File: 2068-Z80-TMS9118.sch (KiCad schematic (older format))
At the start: 39 parts, among them J1 RCJ-014, J2 Conn_02x20_Counter_Clockwise, J3 DB9_Male_MountingHoles, J4 DB9_Male_MountingHoles, J5 Conn_02x10_Odd_Even, J6 Conn_01x02, Q3 2N4401, U1 TMS4416, U2 TMS4416, U3 TMS9118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

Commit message: Change schematic to as-built bodged Rev 0
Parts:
- removed R1: 10, Resistor_THT:R_Axial_DIN0204_L3.6mm_D1.6mm_P5.08mm_Horizontal, symbol Device:R
- removed R2: 10K, Resistor_THT:R_Axial_DIN0204_L3.6mm_D1.6mm_P5.08mm_Horizontal, symbol Device:R
- removed R4: 330, Resistor_THT:R_Axial_DIN0204_L3.6mm_D1.6mm_P5.08mm_Horizontal, symbol Device:R
- added C11: 470pF, Capacitor_THT:C_Disc_D3.8mm_W2.6mm_P2.50mm, symbol Device:C_Small
- added C12, C13: .1uF, Capacitor_THT:C_Disc_D3.8mm_W2.6mm_P2.50mm, symbol Device:C_Small
- added FB1: Ferrite_Bead_Small, Resistor_THT:R_Axial_DIN0204_L3.6mm_D1.6mm_P5.08mm_Horizontal, symbol Device:Ferrite_Bead_Small
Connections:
- net +5V: now also C12.1, C13.1, FB1.1; no longer J3.5, J4.5
- net A8_1: no longer J3.7
- net A9_1: no longer J4.7
- net GND: now also C11.2, C12.2, C13.2; no longer J3.9, J4.9
- net NTSC: now also C11.1
- net at C8.1, C9.1, Q3.3 (C): now also FB1.2
- no-connect marks 30 -> 36
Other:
- note added: "Copyright (C) 2022 John Winans\n\nThis documentation describes Open Hardware and is licensed under the CERN OHL v. 1.2.\n\nYou may redistribute and modify this documentation under the terms of the CERN OHL v.1.2. (http://ohwr.org/cernohl). \nThis documentation is distributed WITHOUT ANY EXPRESS OR IMPLIED WARRANTY, INCLUDING OF MERCHANTABILITY, \nSATISFACTORY QUALITY AND FITNESS FOR A PARTICULAR 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"
- note added: "Down"
- note added: "Fire"
- note added: "Left"
- note added: "Right"
- note added: "Up"
- note removed: "Copyright (C) 2021 John Winans\n\nThis documentation describes Open Hardware and is licensed under the CERN OHL v. 1.2.\n\nYou may redistribute and modify this documentation under the terms of the CERN OHL v.1.2. (http://ohwr.org/cernohl). \nThis documentation is distributed WITHOUT ANY EXPRESS OR IMPLIED WARRANTY, INCLUDING OF MERCHANTABILITY, \nSATISFACTORY QUALITY AND FITNESS FOR A PARTICULAR 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"
- note removed: "Do not populate R2"
- moved on the sheet: J3, J4, J5

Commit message: Added first draft BOM for Rev 1
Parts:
- C1, C10, C12, C13, C2, C3, C6, C8: MPN (none) -> C315C104M5U5TA7303; Manufacturer (none) -> KEMET
- C11: Description CAP CER 0.1UF 50V Z5U RADIAL -> CAP CER 470PF 10% 100V C0G RAD; Digi-Key_PN 399-9859-1-ND‎ -> 399-13987-ND; MPN (none) -> C315C471K1G5TA; Manufacturer (none) -> KEMET
- C4, C5: Description CAP CER 0.1UF 50V Z5U RADIAL -> CAP CER 27PF 10% 200V C0G RADIAL; Digi-Key_PN 399-9859-1-ND‎ -> 399-13983-ND; MPN (none) -> C315C270K2G5TA; Manufacturer (none) -> KEMET
- C7: Description (none) -> 470 µF 10 V Aluminum Electrolytic Capacitors Radial, Can 54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; Digi-Key_PN (none) -> 338-1709-ND; MPN (none) -> SK471M010ST; Manufacturer (none) -> Cornell Dubilier Electronics (CDE)
- C9: Manufacturer (none) -> Panasonic Electronic Components
- D1: Description (none) -> DIODE GEN PURP 100V 200MA DO35; Digi-Key_PN (none) -> 1N914CT-ND; MPN (none) -> 1N914TR; Manufacturer (none) -> onsemi
- FB1: Description (none) -> FERRITE BEAD 50 OHM AXIAL 1LN; Digi-Key_PN (none) -> P9820BK-ND; MPN (none) -> EXC-ELSA35; Manufacturer (none) -> Panasonic Electronic Components
- J2: Description Female connector, double row, 02x20 -> 2 x 20 (40 Pin) Extra Tall Female 0.1 Inch Pitch Stacking H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; Digi-Key_PN S6104-ND -> (none); MPN PPTC202LFBN-RC -> (none); Manufacturer Sullins Connector Solutions -> (none)
- J3, J4: Description (none) -> 9 Position D-Sub Plug, Male Pins Connector; Digi-Key_PN (none) -> AE10970-ND; MPN (none) -> A-DS 09 A/KG-T4S; Manufacturer (none) -> Assmann WSW Components
- J5: Description (none) -> CONN HEADER VERT 20POS 2.54MM; Digi-Key_PN (none) -> 2057-PH2-20-UA-ND; MPN (none) -> PH2-20-UA; Manufacturer (none) -> Adam Tech
- J6: Description (none) -> CONN HEADER VERT 2POS 2.54MM; Digi-Key_PN (none) -> 2057-PH1-02-UA-ND; MPN (none) -> PH1-02-UA; Manufacturer (none) -> Adam Tech
- Q3: Description NPN transistor -> TRANS NPN 40V 0.6A TO92-3; Digi-Key_PN (none) -> 2N4401TFCT-ND; MPN (none) -> 2N4401TF; Manufacturer (none) -> onsemi
- R3: Description RES 1K OHM 5% 1/8W AXIAL -> RES 33 OHM 5% 1/8W AXIAL; Digi-Key_PN CF18JT1K00CT-ND -> CF18JT33R0CT-ND; MPN CF18JT1K00 -> CF18JT33R0
- R7: Description RES 1K OHM 5% 1/8W AXIAL -> RES 470 OHM 5% 1/8W AXIAL; Digi-Key_PN CF18JT1K00CT-ND -> CF18JT470RCT-ND; MPN CF18JT1K00 -> CF18JT470R
- RN1, RN2: Description (none) -> RES ARRAY 8 RES 10K OHM 9SIP; Digi-Key_PN (none) -> 4609X-101-103LF-ND; MPN (none) -> 4609X-101-103LF; Manufacturer (none) -> Bourns Inc.
- U1, U2, U3: MPN (none) -> EBAY
- U4, U5: Description (none) -> IC DECODER/DEMUX 1X3:8 16DIP; Digi-Key_PN (none) -> 296-1639-5-ND; MPN (none) -> SN74LS138N; Manufacturer (none) -> Texas Instruments
- U6, U7: Description (none) -> IC BUF NON-INVERT 5.25V 20DIP; Digi-Key_PN (none) -> 296-1653-5-ND; MPN (none) -> SN74LS244N; Manufacturer (none) -> Texas Instruments
- Y1: Description (none) -> CRYSTAL 10.738635MHZ 32PF TH; Manufacturer (none) -> CTS-Frequency Controls

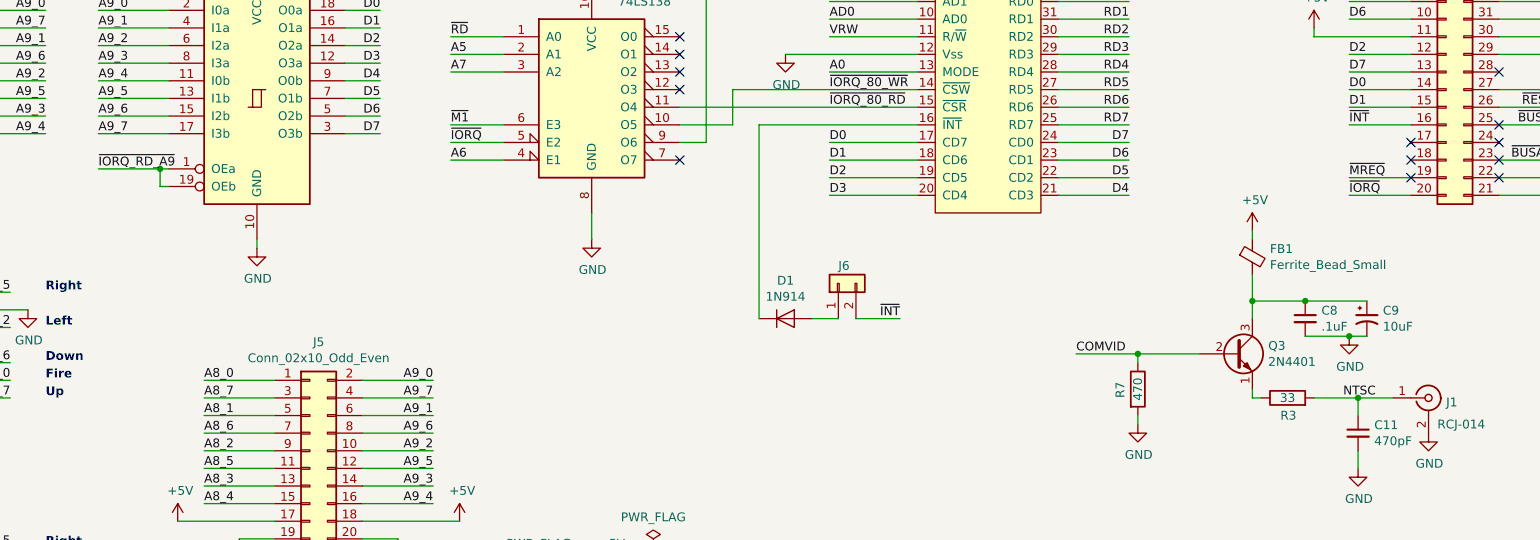
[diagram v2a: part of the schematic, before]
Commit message: Added J7 and replace J6 (to include NMI)
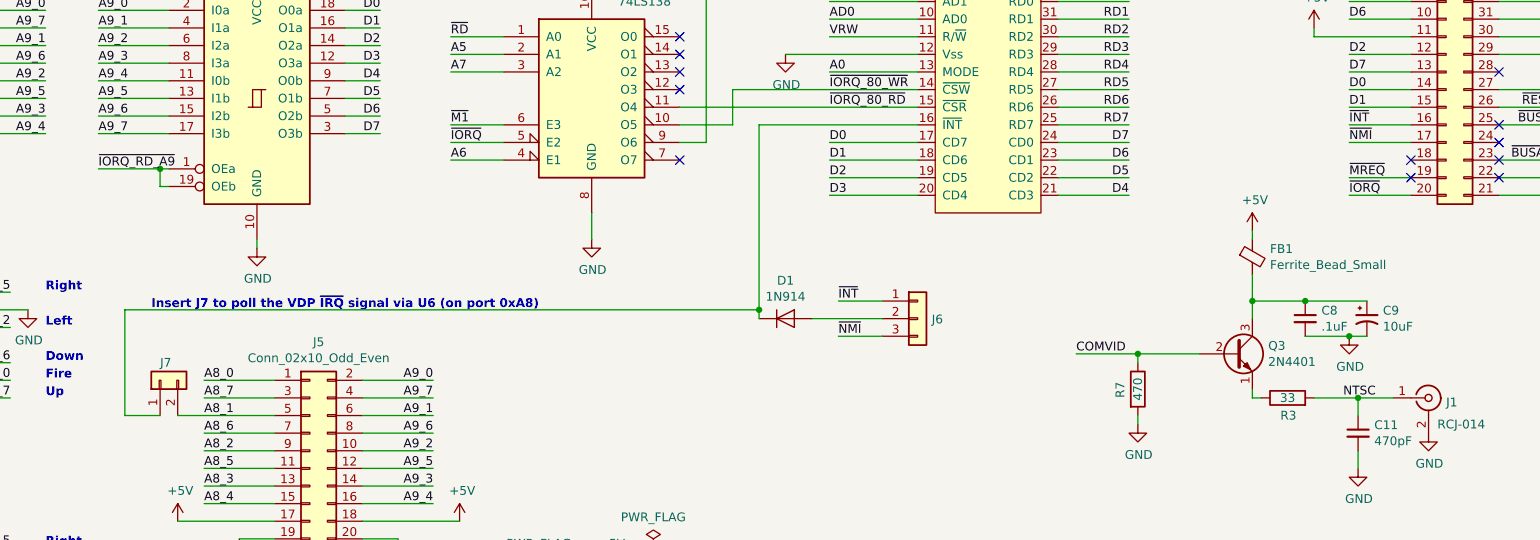
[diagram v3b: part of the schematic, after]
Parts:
- removed J6: Conn_01x02, Connector_PinHeader_2.54mm:PinHeader_1x02_P2.54mm_Vertical, symbol Connector_Generic:Conn_01x02
- added J6: Conn_01x03, Connector_PinHeader_2.54mm:PinHeader_1x03_P2.54mm_Vertical, symbol Connector_Generic:Conn_01x03
- added J7: Conn_01x02, Connector_PinHeader_2.54mm:PinHeader_1x02_P2.54mm_Vertical, symbol Connector_Generic:Conn_01x02
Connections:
- net A8_1: now also J7.2 (Pin_2)
- net ~INT: now also J6.1 (Pin_1)
- net ~NMI: now reaches J2.17 (Pin_17)
- net ~NMI: now also J6.3 (Pin_3)
- net at D1.1 (K), U3.16 (~INT): now also J7.1 (Pin_1)
- net at D1.2 (A): now also J6.2 (Pin_2)
- no-connect marks 36 -> 35
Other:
- note added: "Insert J7 to poll the VDP ~IRQ~ signal via U6 (on port 0xA8)"
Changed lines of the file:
@@
 Sheet 1 1
 Title "TMS9118 Video & Joysticks"
-Date "2021-09-05"
-Rev "1"
+Date "2023-05-20"
+Rev "2"
 Comp ""
 Comment1 ""
@@
 NoConn ~ 9750 4400
 NoConn ~ 9250 4500
-NoConn ~ 9250 4400
 NoConn ~ 9250 3300
 $Comp
@@
 Wire Wire Line
 	2800 6450 2400 6450
-Wire Wire Line
-	2400 5950 2800 5950
 Text Label 2400 5750 0    50   ~ 0
 A8_0
@@
 Text Label 8900 4300 0    50   ~ 0
 ~INT
-Text Label 6350 5400 2    50   ~ 0
+Text Label 6000 5300 0    50   ~ 0
 ~INT
 $Comp
@@
 $EndComp
 Wire Wire Line
-	5850 5400 6000 5400
-Wire Wire Line
-	5550 5400 5550 4300
+	5550 5400 5550 5350
 Wire Wire Line
 	5550 4300 6450 4300
-$Comp
-L Connector_Generic:Conn_01x02 J6
-U 1 1 64FA6625
-P 6000 5200
-F 0 "J6" V 6100 5200 50  0000 R CNN
-F 1 "Conn_01x02" V 5873 5012 50  0001 R CNN
-F 2 "Connector_PinHeader_2.54mm:PinHeader_1x02_P2.54mm_Vertical" H 6000 5200 50  0001 C CNN
-F 3 "https://app.adam-tech.com/products/download/data_sheet/201605/ph1-xx-ua-data-sheet.pdf" H 6000 5200 50  0001 C CNN
-F 4 "CONN HEADER VERT 2POS 2.54MM" H 6000 5200 50  0001 C CNN "Description"
-F 5 "2057-PH1-02-UA-ND" H 6000 5200 50  0001 C CNN "Digi-Key_PN"
-F 6 "PH1-02-UA" H 6000 5200 50  0001 C CNN "MPN"
-F 7 "Adam Tech" H 6000 5200 50  0001 C CNN "Manufacturer"
-	1    6000 5200
-	0    -1   -1   0
-$EndComp
-Wire Wire Line
-	6100 5400 6350 5400
+Wire Wire Line
+	6250 5300 6000 5300
 Wire Wire Line
 	2200 1400 1800 1400
@@
 	2650 7600 2300 7600
 Connection ~ 2650 7600
+$Comp
+L Connector_Generic:Conn_01x02 J7
+U 1 1 646B8B12
+P 2150 5750
+F 0 "J7" V 2250 5750 50  0000 R CNN
+F 1 "Conn_01x02" V 2023 5562 50  0001 R CNN
+F 2 "Connector_PinHeader_2.54mm:PinHeader_1x02_P2.54mm_Vertical" H 2150 5750 50  0001 C CNN
+F 3 "https://app.adam-tech.com/products/download/data_sheet/201605/ph1-xx-ua-data-sheet.pdf" H 2150 5750 50  0001 C CNN
+F 4 "CONN HEADER VERT 2POS 2.54MM" H 2150 5750 50  0001 C CNN "Description"
+F 5 "2057-PH1-02-UA-ND" H 2150 5750 50  0001 C CNN "Digi-Key_PN"
+F 6 "PH1-02-UA" H 2150 5750 50  0001 C CNN "MPN"
+F 7 "Adam Tech" H 2150 5750 50  0001 C CNN "Manufacturer"
+	1    2150 5750
+	0    -1   -1   0
+$EndComp
+Wire Wire Line
+	2250 5950 2800 5950
+Wire Wire Line
+	2150 5950 1950 5950
+Wire Wire Line
+	1950 5950 1950 5350
+Wire Wire Line
+	1950 5350 5550 5350
+Connection ~ 5550 5350
+Wire Wire Line
+	5550 5350 5550 4300
+Text Notes 2100 5350 0    50   ~ 10
+Insert J7 to poll the VDP ~IRQ~ signal via U6 (on port 0xA8)
+$Comp
+L Connector_Generic:Conn_01x03 J6
+U 1 1 647F010F
+P 6450 5400
+F 0 "J6" H 6530 5396 50  0000 L CNN
+F 1 "Conn_01x03" V 6323 5212 50  0001 R CNN
+F 2 "Connector_PinHeader_2.54mm:PinHeader_1x03_P2.54mm_Vertical" H 6450 5400 50  0001 C CNN
+F 3 "~" H 6450 5400 50  0001 C CNN
+	1    6450 5400
+	1    0    0    -1
+$EndComp
+Wire Wire Line
+	5850 5400 6250 5400
+Text Label 6000 5500 0    50   ~ 0
+~NMI
+Wire Wire Line
+	6250 5500 6000 5500
+Wire Wire Line
+	9250 4400 8900 4400
+Text Label 8900 4400 0    50   ~ 0
+~NMI
 $EndSCHEMATC

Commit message: Add support for MSX joysticks
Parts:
- added J8, J9: Conn_01x02, Connector_PinHeader_2.54mm:PinHeader_1x02_P2.54mm_Vertical, symbol Connector_Generic:Conn_01x02
- added R1: 100, Resistor_THT:R_Axial_DIN0207_L6.3mm_D2.5mm_P10.16mm_Horizontal, symbol Device:R
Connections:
- net +5V: now also R1.2
- net A8_4: now also J3.7
- net A9_4: now also J4.7
- net GND: now also J3.9, J4.9
- net at J3.5: now also J9.1 (Pin_1)
- net at J4.5: now also J8.1 (Pin_1)
- new net: J8.2 (Pin_2), J9.2 (Pin_2), R1.1
- no-connect marks 35 -> 29
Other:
- note added: "Btn 2"
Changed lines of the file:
@@
 Sheet 1 1
 Title "TMS9118 Video & Joysticks"
-Date "2023-05-20"
-Rev "2"
+Date "2023-06-03"
+Rev "2.1"
 Comp ""
 Comment1 ""
@@
 Text Label 1500 2100 2    50   ~ 0
 A8_4
-$Comp
-L Connector:DB9_Male_MountingHoles J4
-U 1 1 63B67655
-P 750 6900
-F 0 "J4" H 800 7400 50  0000 C CNN
-F 1 "DB9_Male_MountingHoles" H 930 6900 50  0001 L CNN
-F 2 "Connector_Dsub:DSUB-9_Male_Horizontal_P2.77x2.84mm_EdgePinOffset7.70mm_Housed_MountingHolesOffset9.12mm" H 750 6900 50  0001 C CNN
-F 3 "http://www.assmann-wsw.com/uploads/datasheets/ASS_4888_CO.pdf" H 750 6900 50  0001 C CNN
-F 4 "9 Position D-Sub Plug, Male Pins Connector" H 750 6900 50  0001 C CNN "Description"
-F 5 "AE10970-ND" H 750 6900 50  0001 C CNN "Digi-Key_PN"
-F 6 "A-DS 09 A/KG-T4S" H 750 6900 50  0001 C CNN "MPN"
-F 7 "Assmann WSW Components" H 750 6900 50  0001 C CNN "Manufacturer"
-	1    750  6900
-	-1   0    0    -1
-$EndComp
 Wire Wire Line
 	1500 3750 1100 3750
@@
 $EndComp
 Wire Wire Line
-	1050 5350 1400 5350
-Wire Wire Line
-	1050 6800 1400 6800
+	1050 5350 1100 5350
+Wire Wire Line
+	1050 6800 1100 6800
 Wire Wire Line
 	1050 6700 1300 6700
@@
 Text Notes 1500 5850 0    50   ~ 10
 Up
-NoConn ~ 1050 5550
-NoConn ~ 1050 5150
-$Comp
-L Connector:DB9_Male_MountingHoles J3
-U 1 1 6392BF40
-P 750 5450
-F 0 "J3" H 800 5950 50  0000 C CNN
-F 1 "DB9_Male_MountingHoles" H 930 5450 50  0001 L CNN
-F 2 "Connector_Dsub:DSUB-9_Male_Horizontal_P2.77x2.84mm_EdgePinOffset7.70mm_Housed_MountingHolesOffset9.12mm" H 750 5450 50  0001 C CNN
-F 3 "http://www.assmann-wsw.com/uploads/datasheets/ASS_4888_CO.pdf" H 750 5450 50  0001 C CNN
-F 4 "9 Position D-Sub Plug, Male Pins Connector" H 750 5450 50  0001 C CNN "Description"
-F 5 "AE10970-ND" H 750 5450 50  0001 C CNN "Digi-Key_PN"
-F 6 "A-DS 09 A/KG-T4S" H 750 5450 50  0001 C CNN "MPN"
-F 7 "Assmann WSW Components" H 750 5450 50  0001 C CNN "Manufacturer"
-	1    750  5450
-	-1   0    0    -1
-$EndComp
-NoConn ~ 1050 5050
 Text Notes 1500 5650 0    50   ~ 10
 Down
@@
 Text Notes 1500 7200 0    50   ~ 10
 Fire
-NoConn ~ 1050 6500
-NoConn ~ 1050 6600
-NoConn ~ 1050 7000
 Wire Wire Line
 	7700 5600 8050 5600
@@
 Text Label 8900 4400 0    50   ~ 0
 ~NMI
+$Comp
+L Connector_Generic:Conn_01x02 J8
+U 1 1 64804C73
+P 1200 6250
+F 0 "J8" V 1300 6250 50  0000 R CNN
+F 1 "Conn_01x02" V 1073 6062 50  0001 R CNN
+F 2 "Connector_PinHeader_2.54mm:PinHeader_1x02_P2.54mm_Vertical" H 1200 6250 50  0001 C CNN
+F 3 "https://app.adam-tech.com/products/download/data_sheet/201605/ph1-xx-ua-data-sheet.pdf" H 1200 6250 50  0001 C CNN
+F 4 "CONN HEADER VERT 2POS 2.54MM" H 1200 6250 50  0001 C CNN "Description"
+F 5 "2057-PH1-02-UA-ND" H 1200 6250 50  0001 C CNN "Digi-Key_PN"
+F 6 "PH1-02-UA" H 1200 6250 50  0001 C CNN "MPN"
+F 7 "Adam Tech" H 1200 6250 50  0001 C CNN "Manufacturer"
+	1    1200 6250
+	0    -1   -1   0
+$EndComp
+$Comp
+L Connector:DB9_Male_MountingHoles J4
+U 1 1 63B67655
+P 750 6900
+F 0 "J4" H 800 7400 50  0000 C CNN
+F 1 "DB9_Male_MountingHoles" H 930 6900 50  0001 L CNN
+F 2 "Connector_Dsub:DSUB-9_Male_Horizontal_P2.77x2.84mm_EdgePinOffset7.70mm_Housed_MountingHolesOffset9.12mm" H 750 6900 50  0001 C CNN
+F 3 "http://www.assmann-wsw.com/uploads/datasheets/ASS_4888_CO.pdf" H 750 6900 50  0001 C CNN
+F 4 "9 Position D-Sub Plug, Male Pins Connector" H 750 6900 50  0001 C CNN "Description"
+F 5 "AE10970-ND" H 750 6900 50  0001 C CNN "Digi-Key_PN"
+F 6 "A-DS 09 A/KG-T4S" H 750 6900 50  0001 C CNN "MPN"
+F 7 "Assmann WSW Components" H 750 6900 50  0001 C CNN "Manufacturer"
+	1    750  6900
+	-1   0    0    -1
+$EndComp
+$Comp
+L Connector:DB9_Male_MountingHoles J3
+U 1 1 6392BF40
+P 750 5450
+F 0 "J3" H 800 5950 50  0000 C CNN
+F 1 "DB9_Male_MountingHoles" H 930 5450 50  0001 L CNN
+F 2 "Connector_Dsub:DSUB-9_Male_Horizontal_P2.77x2.84mm_EdgePinOffset7.70mm_Housed_MountingHolesOffset9.12mm" H 750 5450 50  0001 C CNN
+F 3 "http://www.assmann-wsw.com/uploads/datasheets/ASS_4888_CO.pdf" H 750 5450 50  0001 C CNN
+F 4 "9 Position D-Sub Plug, Male Pins Connector" H 750 5450 50  0001 C CNN "Description"
+F 5 "AE10970-ND" H 750 5450 50  0001 C CNN "Digi-Key_PN"
+F 6 "A-DS 09 A/KG-T4S" H 750 5450 50  0001 C CNN "MPN"
+F 7 "Assmann WSW Components" H 750 5450 50  0001 C CNN "Manufacturer"
+	1    750  5450
+	-1   0    0    -1
+$EndComp
+Wire Wire Line
+	1050 6500 1200 6500
+Wire Wire Line
+	1200 6500 1200 6450
+Wire Wire Line
+	1300 6450 1400 6450
+$Comp
+L power:+5V #PWR0124
+U 1 1 6485FD29
+P 1950 6450
+F 0 "#PWR0124" H 1950 6300 50  0001 C CNN
+F 1 "+5V" H 1965 6623 50  0000 C CNN
+F 2 "" H 1950 6450 50  0001 C CNN
+F 3 "" H 1950 6450 50  0001 C CNN
+	1    1950 6450
+	1    0    0    -1
+$EndComp
+$Comp
+L Device:R R1
+U 1 1 648995F2
+P 1700 6450
+F 0 "R1" V 1600 6400 50  0000 L CNN
+F 1 "100" V 1700 6450 50  0000 C CNN
+F 2 "Resistor_THT:R_Axial_DIN0207_L6.3mm_D2.5mm_P10.16mm_Horizontal" V 1630 6450 50  0001 C CNN
+F 3 "https://www.seielect.com/catalog/sei-cf_cfm.pdf" H 1700 6450 50  0001 C CNN
+F 4 "RES 33 OHM 5% 1/8W AXIAL" H 1700 6450 50  0001 C CNN "Description"
+F 5 "CF18JT33R0CT-ND" H 1700 6450 50  0001 C CNN "Digi-Key_PN"
+F 6 "CF18JT33R0" H 1700 6450 50  0001 C CNN "MPN"
+F 7 "Stackpole Electronics Inc" H 1700 6450 50  0001 C CNN "Manufacturer"
+	1    1700 6450
+	0    -1   -1   0
+$EndComp
+Wire Wire Line
+	1850 6450 1950 6450
+$Comp
+L Connector_Generic:Conn_01x02 J9
+U 1 1 648D087B
+P 1150 4750
+F 0 "J9" V 1250 4750 50  0000 R CNN
+F 1 "Conn_01x02" V 1023 4562 50  0001 R CNN
+F 2 "Connector_PinHeader_2.54mm:PinHeader_1x02_P2.54mm_Vertical" H 1150 4750 50  0001 C CNN
+F 3 "https://app.adam-tech.com/products/download/data_sheet/201605/ph1-xx-ua-data-sheet.pdf" H 1150 4750 50  0001 C CNN
+F 4 "CONN HEADER VERT 2POS 2.54MM" H 1150 4750 50  0001 C CNN "Description"
+F 5 "2057-PH1-02-UA-ND" H 1150 4750 50  0001 C CNN "Digi-Key_PN"
+F 6 "PH1-02-UA" H 1150 4750 50  0001 C CNN "MPN"
+F 7 "Adam Tech" H 1150 4750 50  0001 C CNN "Manufacturer"
+	1    1150 4750
+	0    -1   -1   0
+$EndComp
+Wire Wire Line
+	1050 5050 1150 5050
+Wire Wire Line
+	1150 5050 1150 4950
+Wire Wire Line
+	1250 4950 1800 4950
+Wire Wire Line
+	1800 4950 1800 6150
+Wire Wire Line
+	1800 6150 1400 6150
+Wire Wire Line
+	1400 6150 1400 6450
+Wire Wire Line
+	1400 6450 1550 6450
+Connection ~ 1400 6450
+Wire Wire Line
+	1050 5150 1100 5150
+Wire Wire Line
+	1100 5150 1100 5350
+Connection ~ 1100 5350
+Wire Wire Line
+	1100 5350 1400 5350
+Wire Wire Line
+	1050 6600 1100 6600
+Wire Wire Line
+	1100 6600 1100 6800
+Connection ~ 1100 6800
+Wire Wire Line
+	1100 6800 1400 6800
+Wire Wire Line
+	1050 7000 1300 7000
+Text Label 1300 7000 2    50   ~ 0
+A9_4
+Wire Wire Line
+	1050 5550 1300 5550
+Text Label 1300 5550 2    50   ~ 0
+A8_4
+Text Notes 1500 5550 0    50   ~ 10
+Btn 2
+Text Notes 1500 7000 0    50   ~ 10
+Btn 2
 $EndSCHEMATC
